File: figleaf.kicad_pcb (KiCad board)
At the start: 2 copper layers, 150 x 105 mm, 31 parts, among them U1 Nice_Nano_V2_GRAZ

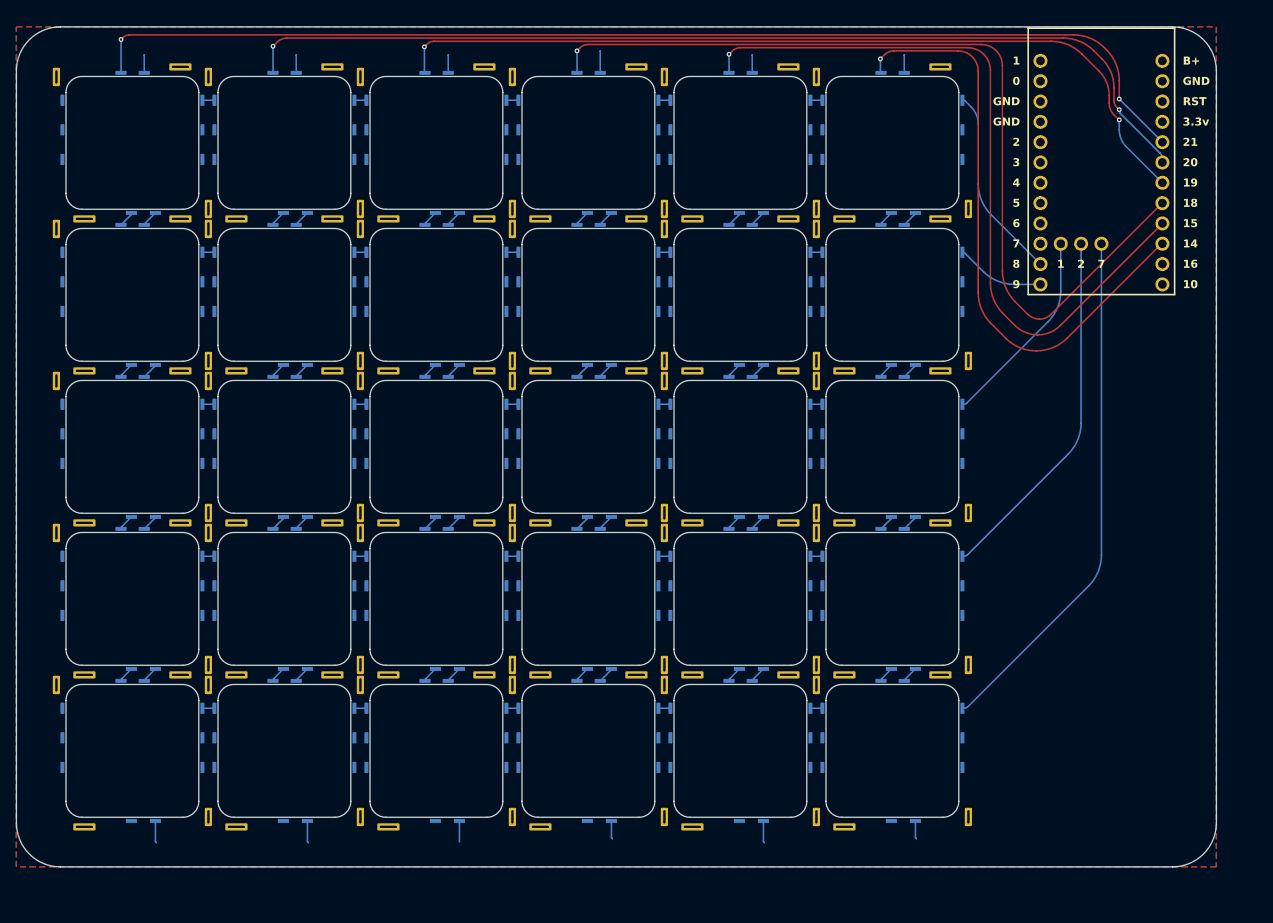
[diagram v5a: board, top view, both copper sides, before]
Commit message: Add n!n SMD variant
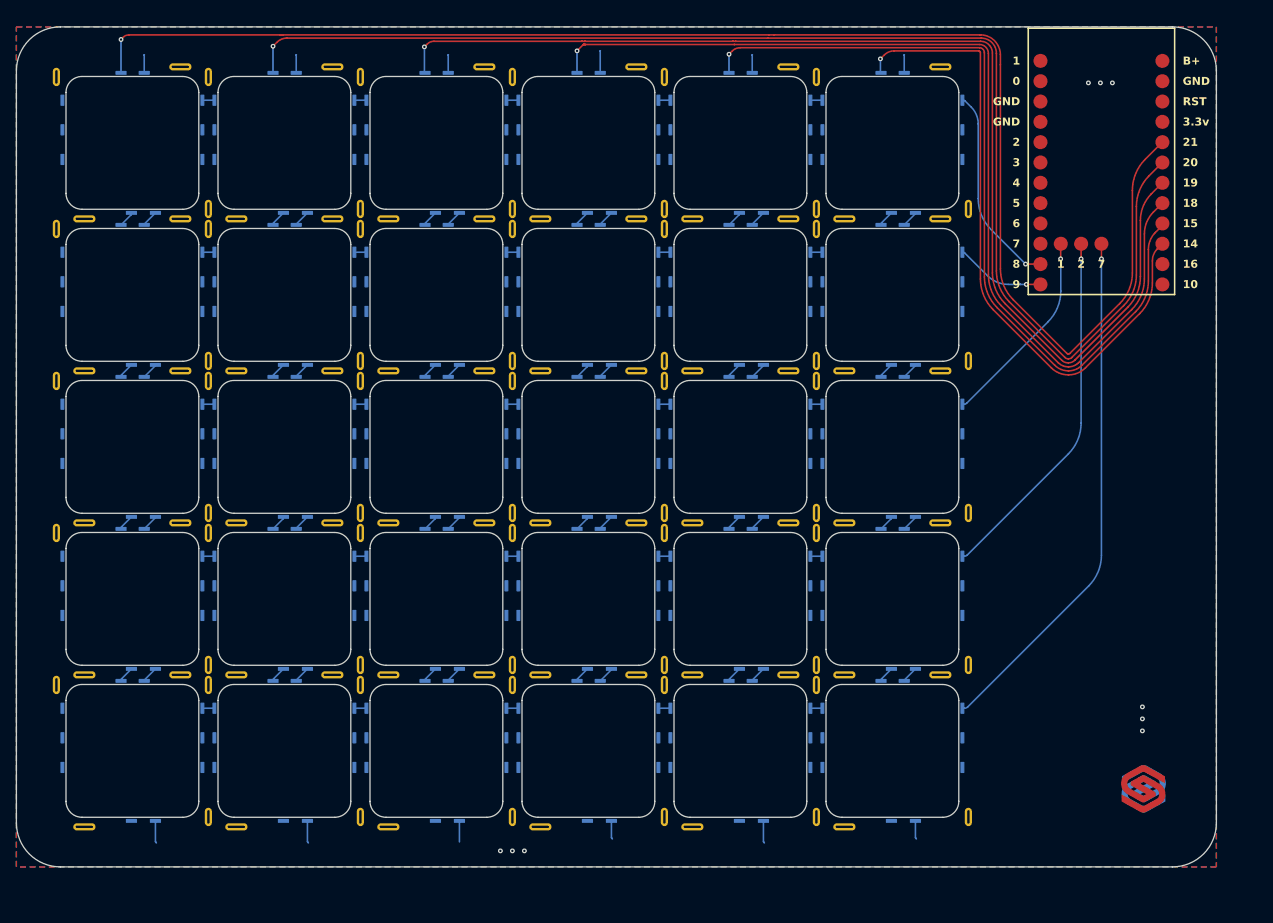
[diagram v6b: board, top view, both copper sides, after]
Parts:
- U1: footprint MCU:Nice_Nano_V2 -> Graz_Footprints:Nice_Nano_V2_Graz
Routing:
- net col_0: track 142.2 -> 187.4 mm, vias 2 -> 1
- net col_1: track 123.8 -> 165.9 mm, vias 2 -> 1
- net col_2: track 105.9 -> 145.0 mm, vias 2 -> 1
- net col_3: track 112.7 -> 123.7 mm
- net col_4: track 94.1 -> 102.5 mm
- net col_5: track 75.6 -> 81.5 mm
- net row_0: track 24.3 -> 25.3 mm, vias 0 -> 1
- net row_1: vias 0 -> 1
- net row_2: vias 0 -> 1
- net GND_L: vias 0 -> 9
- net row_4: vias 0 -> 1
- net row_3: vias 0 -> 1

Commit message: PCB cleanup
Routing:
- net row_2: track 25.1 -> 26.5 mm
- net row_4: track 65.3 -> 64.6 mm

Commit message: Add power components v1
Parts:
- added H1: M1.6_mounting, Graz_Footprints:m1.6, F.Cu at (23.3, 23.3)
- added H2: M1.6_mounting, Graz_Footprints:m1.6, F.Cu at (166.8, 23.3)
- added H3: M1.6_mounting, Graz_Footprints:m1.6, F.Cu at (23.3, 121.7)
- added H4: M1.6_mounting, Graz_Footprints:m1.6, F.Cu at (166.8, 121.7)
- added L_J1: Conn_01x02_Socket, Connector_JST:JST_SH_SM02B-SRSS-TB_1x02-1MP_P1.00mm_Horizontal, F.Cu at (151.2, 56.8)
- added L_RSW1: SW_RST, Button_Switch_SMD:SW_Tactile_SPST_NO_Straight_CK_PTS636Sx25SMTRLFS, F.Cu at (163.0, 59.0)
- added L_SW1: SW_SPDT, Button_Switch_SMD:SW_SPDT_PCM12, F.Cu at (141.8, 21.9)
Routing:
- net +BATT_L: track 0.00 -> 35.5 mm, vias 0 -> 2
- net GND_L: track 29.6 -> 0.00 mm, vias 9 -> 11
- net RESET_L: track 0.00 -> 27.2 mm
- net RAW_L: track 0.00 -> 24.6 mm, vias 0 -> 2
- net col_4: track 102.5 -> 98.5 mm
- net col_3: track 123.7 -> 119.9 mm
- net col_2: track 145.0 -> 141.2 mm
- net col_1: track 165.9 -> 162.2 mm
- net col_5: track 81.4 -> 77.8 mm
- net col_0: track 187.1 -> 188.1 mm
